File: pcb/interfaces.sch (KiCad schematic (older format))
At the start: 14 parts

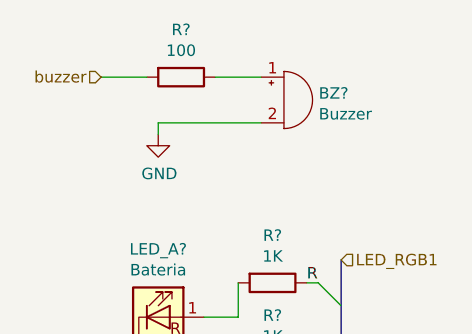
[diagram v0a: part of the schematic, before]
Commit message: Increased Resistance
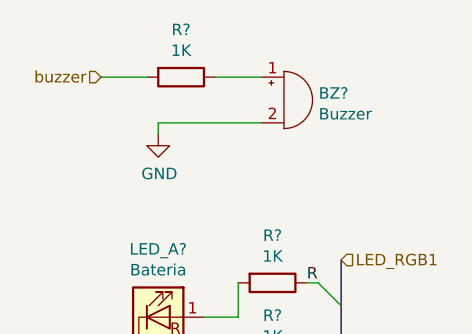
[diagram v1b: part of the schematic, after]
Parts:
- R?: value 100 -> 1K
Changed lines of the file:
@@
 Wire Wire Line
 	1650 1200 1650 1250
-$Comp
-L Device:R R?
-U 1 1 5D37B34E
-P 1750 1000
-F 0 "R?" V 1543 1000 50  0000 C CNN
-F 1 "100" V 1634 1000 50  0000 C CNN
-F 2 "" V 1680 1000 50  0001 C CNN
-F 3 "~" H 1750 1000 50  0001 C CNN
-	1    1750 1000
-	0    1    1    0
-$EndComp
 Wire Wire Line
 	1900 1000 2100 1000
@@
 Text Label 2300 2600 0    50   ~ 0
 B
-Wire Bus Line
-	2450 3900 2450 4650
-Wire Bus Line
-	2450 2900 2450 3650
-Wire Bus Line
-	2450 1800 2450 2700
 $Comp
 L power:GND #PWR?
@@
 	1    0    0    -1
 $EndComp
+Wire Bus Line
+	2450 1800 2450 2700
+Wire Bus Line
+	2450 2900 2450 3650
+Wire Bus Line
+	2450 3900 2450 4650
+$Comp
+L Device:R R?
+U 1 1 5D37B34E
+P 1750 1000
+F 0 "R?" V 1543 1000 50  0000 C CNN
+F 1 "1K" V 1634 1000 50  0000 C CNN
+F 2 "" V 1680 1000 50  0001 C CNN
+F 3 "~" H 1750 1000 50  0001 C CNN
+	1    1750 1000
+	0    1    1    0
+$EndComp
 $EndSCHEMATC

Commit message: Fix and Anotate design
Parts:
- gave numbers to parts that had none: 14
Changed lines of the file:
@@
 EESchema Schematic File Version 4
-LIBS:rasbot-cache
 EELAYER 29 0
 EELAYER END
@@
 $EndDescr
 $Comp
-L Device:LED_RCBG LED_A?
+L Device:LED_RCBG LED_A1
 U 1 1 5D35DFE4
 P 1650 2250
-F 0 "LED_A?" H 1650 2747 50  0000 C CNN
+F 0 "LED_A1" H 1650 2747 50  0000 C CNN
 F 1 "Bateria" H 1650 2656 50  0000 C CNN
 F 2 "" H 1650 2200 50  0001 C CNN
@@
 $EndComp
 $Comp
-L Device:LED_RCBG LED_B?
+L Device:LED_RCBG LED_B1
 U 1 1 5D35FAFC
 P 1650 3250
-F 0 "LED_B?" H 1650 3747 50  0000 C CNN
+F 0 "LED_B1" H 1650 3747 50  0000 C CNN
 F 1 "Status1" H 1650 3656 50  0000 C CNN
 F 2 "" H 1650 3200 50  0001 C CNN
@@
 $EndComp
 $Comp
-L Device:Buzzer BZ?
+L Device:Buzzer BZ1
 U 1 1 5D3659BF
 P 2200 1100
-F 0 "BZ?" H 2352 1129 50  0000 L CNN
+F 0 "BZ1" H 2352 1129 50  0000 L CNN
 F 1 "Buzzer" H 2352 1038 50  0000 L CNN
 F 2 "" V 2175 1200 50  0001 C CNN
@@
 	1300 2250 1450 2250
 $Comp
-L Device:R R?
+L Device:R R62
 U 1 1 5D36D747
 P 2150 1900
-F 0 "R?" V 1943 1900 50  0000 C CNN
+F 0 "R62" V 1943 1900 50  0000 C CNN
 F 1 "1K" V 2034 1900 50  0000 C CNN
 F 2 "" V 2080 1900 50  0001 C CNN
@@
 $EndComp
 $Comp
-L Device:R R?
+L Device:R R63
 U 1 1 5D36E108
 P 2150 2250
-F 0 "R?" V 1943 2250 50  0000 C CNN
+F 0 "R63" V 1943 2250 50  0000 C CNN
 F 1 "1K" V 2034 2250 50  0000 C CNN
 F 2 "" V 2080 2250 50  0001 C CNN
@@
 $EndComp
 $Comp
-L Device:R R?
+L Device:R R64
 U 1 1 5D36E671
 P 2150 2600
-F 0 "R?" V 1943 2600 50  0000 C CNN
+F 0 "R64" V 1943 2600 50  0000 C CNN
 F 1 "1K" V 2034 2600 50  0000 C CNN
 F 2 "" V 2080 2600 50  0001 C CNN
@@
 	2000 2450 2000 2600
 $Comp
-L Device:R R?
+L Device:R R65
 U 1 1 5D371663
 P 2150 2950
-F 0 "R?" V 1943 2950 50  0000 C CNN
+F 0 "R65" V 1943 2950 50  0000 C CNN
 F 1 "1K" V 2034 2950 50  0000 C CNN
 F 2 "" V 2080 2950 50  0001 C CNN
@@
 $EndComp
 $Comp
-L Device:R R?
+L Device:R R66
 U 1 1 5D371E66
 P 2150 3250
-F 0 "R?" V 1943 3250 50  0000 C CNN
+F 0 "R66" V 1943 3250 50  0000 C CNN
 F 1 "1K" V 2034 3250 50  0000 C CNN
 F 2 "" V 2080 3250 50  0001 C CNN
@@
 $EndComp
 $Comp
-L Device:R R?
+L Device:R R67
 U 1 1 5D37238B
 P 2150 3550
-F 0 "R?" V 1943 3550 50  0000 C CNN
+F 0 "R67" V 1943 3550 50  0000 C CNN
 F 1 "1K" V 2034 3550 50  0000 C CNN
 F 2 "" V 2080 3550 50  0001 C CNN
@@
 	1850 3250 2000 3250
 $Comp
-L Device:R R?
+L Device:R R69
 U 1 1 5D374F3E
 P 2150 4250
-F 0 "R?" V 1943 4250 50  0000 C CNN
+F 0 "R69" V 1943 4250 50  0000 C CNN
 F 1 "1K" V 2034 4250 50  0000 C CNN
 F 2 "" V 2080 4250 50  0001 C CNN
@@
 $EndComp
 $Comp
-L Device:R R?
+L Device:R R70
 U 1 1 5D37541B
 P 2150 4550
-F 0 "R?" V 1943 4550 50  0000 C CNN
+F 0 "R70" V 1943 4550 50  0000 C CNN
 F 1 "1K" V 2034 4550 50  0000 C CNN
 F 2 "" V 2080 4550 50  0001 C CNN
@@
 	1300 4250 1450 4250
 $Comp
-L Device:R R?
+L Device:R R68
 U 1 1 5D3747B2
 P 2150 3950
-F 0 "R?" V 1943 3950 50  0000 C CNN
+F 0 "R68" V 1943 3950 50  0000 C CNN
 F 1 "1K" V 2034 3950 50  0000 C CNN
 F 2 "" V 2080 3950 50  0001 C CNN
@@
 $EndComp
 $Comp
-L Device:LED_RCBG LED_C?
+L Device:LED_RCBG LED_C1
 U 1 1 5D360961
 P 1650 4250
-F 0 "LED_C?" H 1650 4747 50  0000 C CNN
+F 0 "LED_C1" H 1650 4747 50  0000 C CNN
 F 1 "Status2" H 1650 4656 50  0000 C CNN
 F 2 "" H 1650 4200 50  0001 C CNN
@@
 B
 $Comp
-L power:GND #PWR?
+L power:GND #PWR0163
 U 1 1 5D3B8045
 P 1300 4350
-F 0 "#PWR?" H 1300 4100 50  0001 C CNN
+F 0 "#PWR0163" H 1300 4100 50  0001 C CNN
 F 1 "GND" H 1305 4177 50  0000 C CNN
 F 2 "" H 1300 4350 50  0001 C CNN
@@
 $EndComp
 $Comp
-L power:GND #PWR?
+L power:GND #PWR0162
 U 1 1 5D3B8345
 P 1300 3350
-F 0 "#PWR?" H 1300 3100 50  0001 C CNN
+F 0 "#PWR0162" H 1300 3100 50  0001 C CNN
 F 1 "GND" H 1305 3177 50  0000 C CNN
 F 2 "" H 1300 3350 50  0001 C CNN
@@
 $EndComp
 $Comp
-L power:GND #PWR?
+L power:GND #PWR0161
 U 1 1 5D3B8E0B
 P 1300 2300
-F 0 "#PWR?" H 1300 2050 50  0001 C CNN
+F 0 "#PWR0161" H 1300 2050 50  0001 C CNN
 F 1 "GND" H 1305 2127 50  0000 C CNN
 F 2 "" H 1300 2300 50  0001 C CNN
@@
 $EndComp
 $Comp
-L power:GND #PWR?
+L power:GND #PWR0164
 U 1 1 5D3B9150
 P 1650 1250
-F 0 "#PWR?" H 1650 1000 50  0001 C CNN
+F 0 "#PWR0164" H 1650 1000 50  0001 C CNN
 F 1 "GND" H 1655 1077 50  0000 C CNN
 F 2 "" H 1650 1250 50  0001 C CNN
@@
 	2450 3900 2450 4650
 $Comp
-L Device:R R?
+L Device:R R61
 U 1 1 5D37B34E
 P 1750 1000
-F 0 "R?" V 1543 1000 50  0000 C CNN
+F 0 "R61" V 1543 1000 50  0000 C CNN
 F 1 "1K" V 1634 1000 50  0000 C CNN
 F 2 "" V 1680 1000 50  0001 C CNN

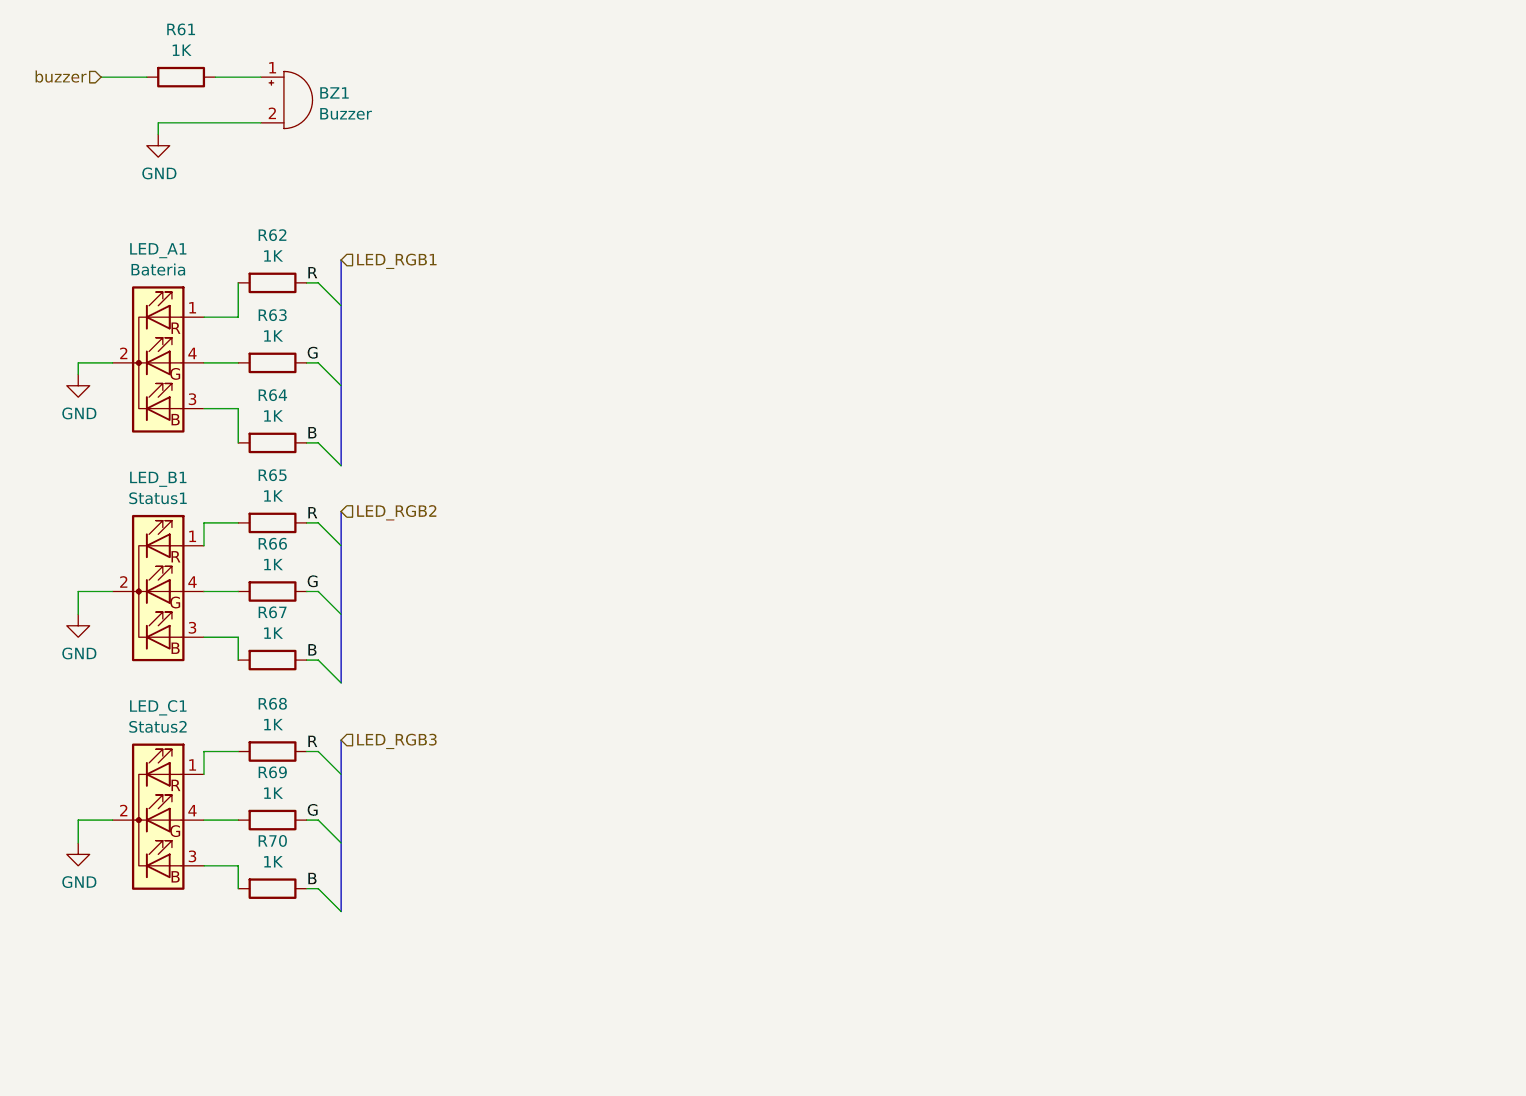
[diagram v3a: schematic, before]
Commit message: MCU connections, OLED and Sonar
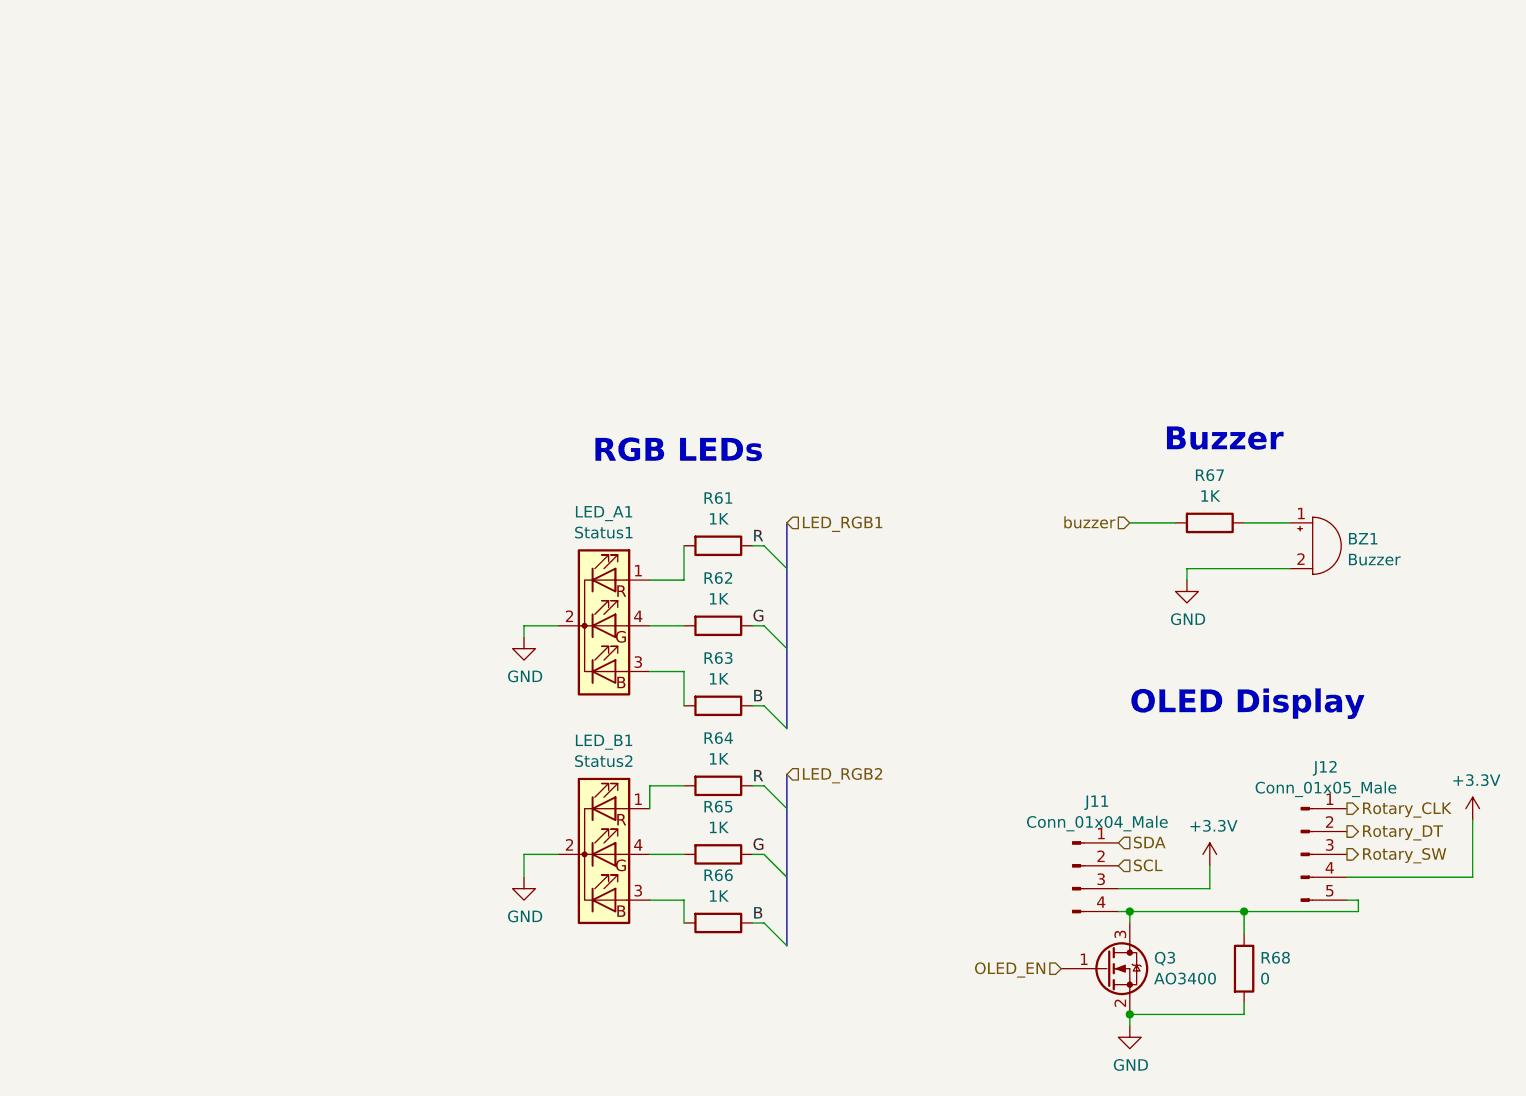
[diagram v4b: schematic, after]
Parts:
- removed LED_C1: Status2, symbol Device:LED_RCBG
- removed R69, R70: 1K, symbol Device:R
- added J11: Conn_01x04_Male, Connector_PinHeader_2.54mm:PinHeader_1x04_P2.54mm_Vertical, symbol Connector:Conn_01x04_Male
- added J12: Conn_01x05_Male, Connector_PinHeader_2.54mm:PinHeader_1x05_P2.54mm_Vertical, symbol Connector:Conn_01x05_Male
- added Q3: AO3400, Package_TO_SOT_SMD:SOT-23, symbol rasbot:AO3400
- BZ1: footprint (none) -> Buzzer_Beeper:Buzzer_12x9.5RM7.6
- LED_A1: value Bateria -> Status1; footprint (none) -> Connector_PinHeader_2.54mm:PinHeader_1x04_P2.54mm_Vertical
- LED_B1: value Status1 -> Status2; footprint (none) -> Connector_PinHeader_2.54mm:PinHeader_1x04_P2.54mm_Vertical
- R61: renamed from R62; footprint (none) -> Resistor_SMD:R_0805_2012Metric
- R62: renamed from R63; footprint (none) -> Resistor_SMD:R_0805_2012Metric
- R63: renamed from R64; footprint (none) -> Resistor_SMD:R_0805_2012Metric
- R64: renamed from R65; footprint (none) -> Resistor_SMD:R_0805_2012Metric
- R65: renamed from R66; footprint (none) -> Resistor_SMD:R_0805_2012Metric
- R66: renamed from R67; footprint (none) -> Resistor_SMD:R_0805_2012Metric
- R67: renamed from R61; footprint (none) -> Resistor_SMD:R_0805_2012Metric
- R68: value 1K -> 0; footprint (none) -> Resistor_SMD:R_0805_2012Metric
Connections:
- net GND: now also R68.2, Q3.2 (S)
- net R: no longer R68.1
- new net: J11.4 (Pin_4), J12.5 (Pin_5), Q3.3 (D), R68.1
- new net +3V3: J11.3 (Pin_3), J12.4 (Pin_4)
- new net OLED_EN: Q3.1 (G)
- new net Rotary_CLK: J12.1 (Pin_1)
- new net Rotary_DT: J12.2 (Pin_2)
- new net Rotary_SW: J12.3 (Pin_3)
- new net SCL: J11.2 (Pin_2)
- new net SDA: J11.1 (Pin_1)
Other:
- note added: "Buzzer"
- note added: "OLED Display"
- note added: "RGB LEDs"
- moved on the sheet: BZ1, LED_A1, LED_B1, R61, R62, R63, R64, R65, R66, R67
